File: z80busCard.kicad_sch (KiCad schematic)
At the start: 14 parts, among them J1 Conn_02x20_Odd_Even, J2 Conn_02x20_Odd_Even, J3 Conn_02x20_Odd_Even, J4 Conn_02x20_Odd_Even, J5 USB_C_Receptacle_PowerOnly_6P, SW1 SW_Push

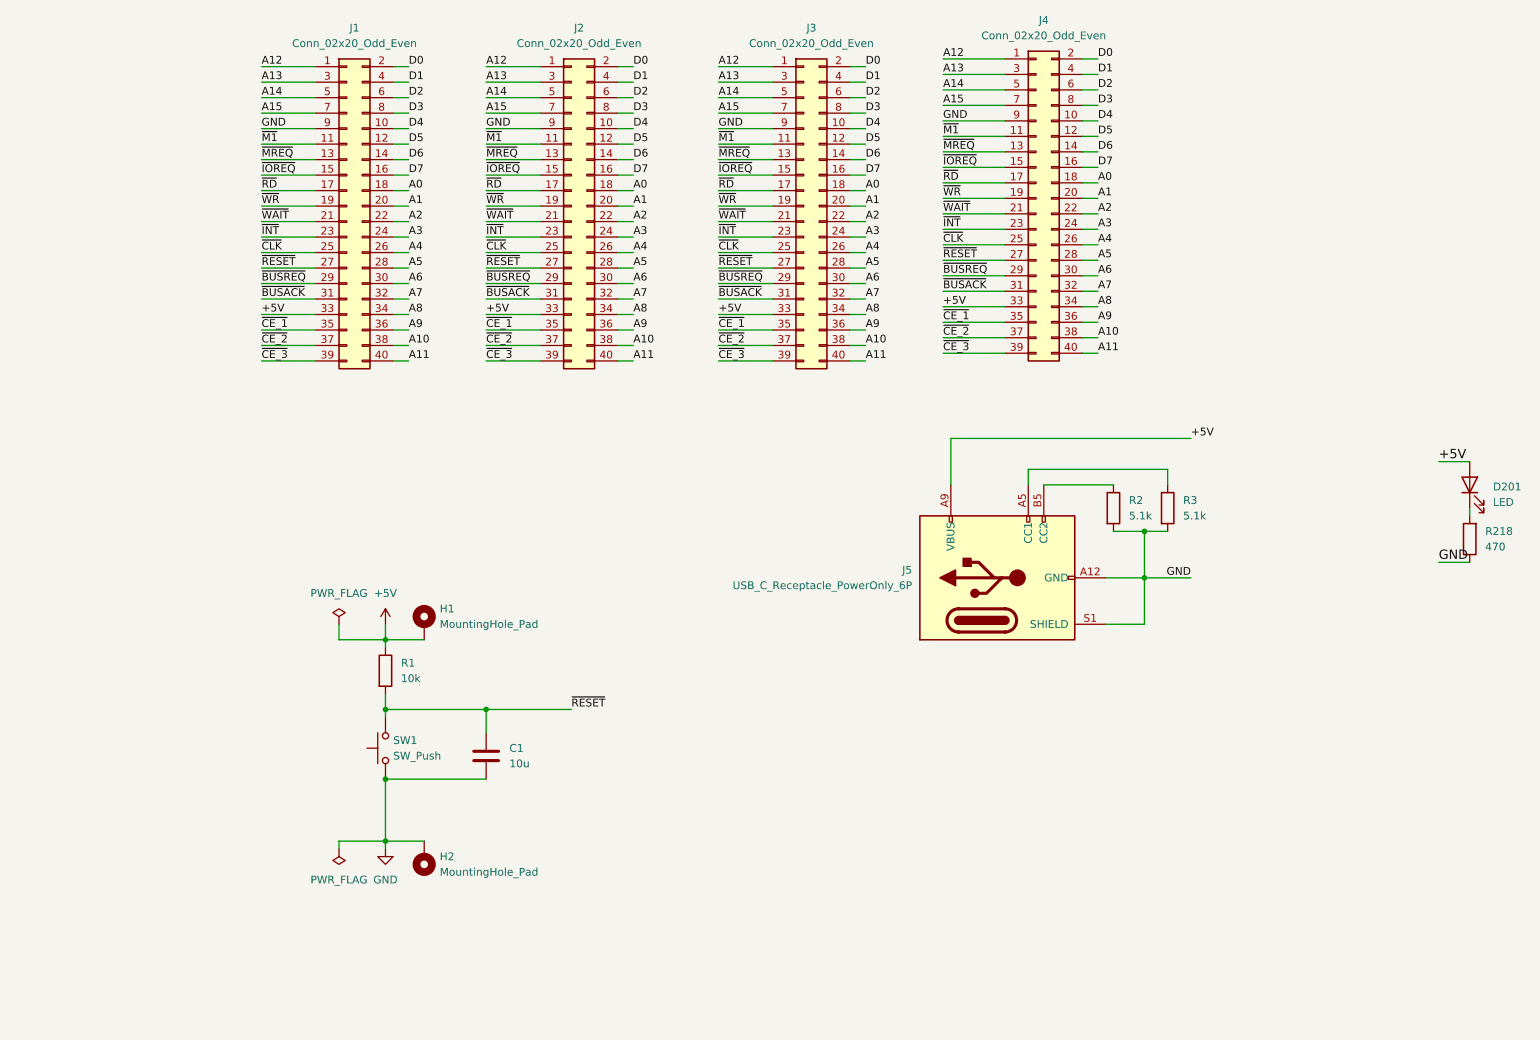
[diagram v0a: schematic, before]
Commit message: Add RESET inputs and signal conditioning
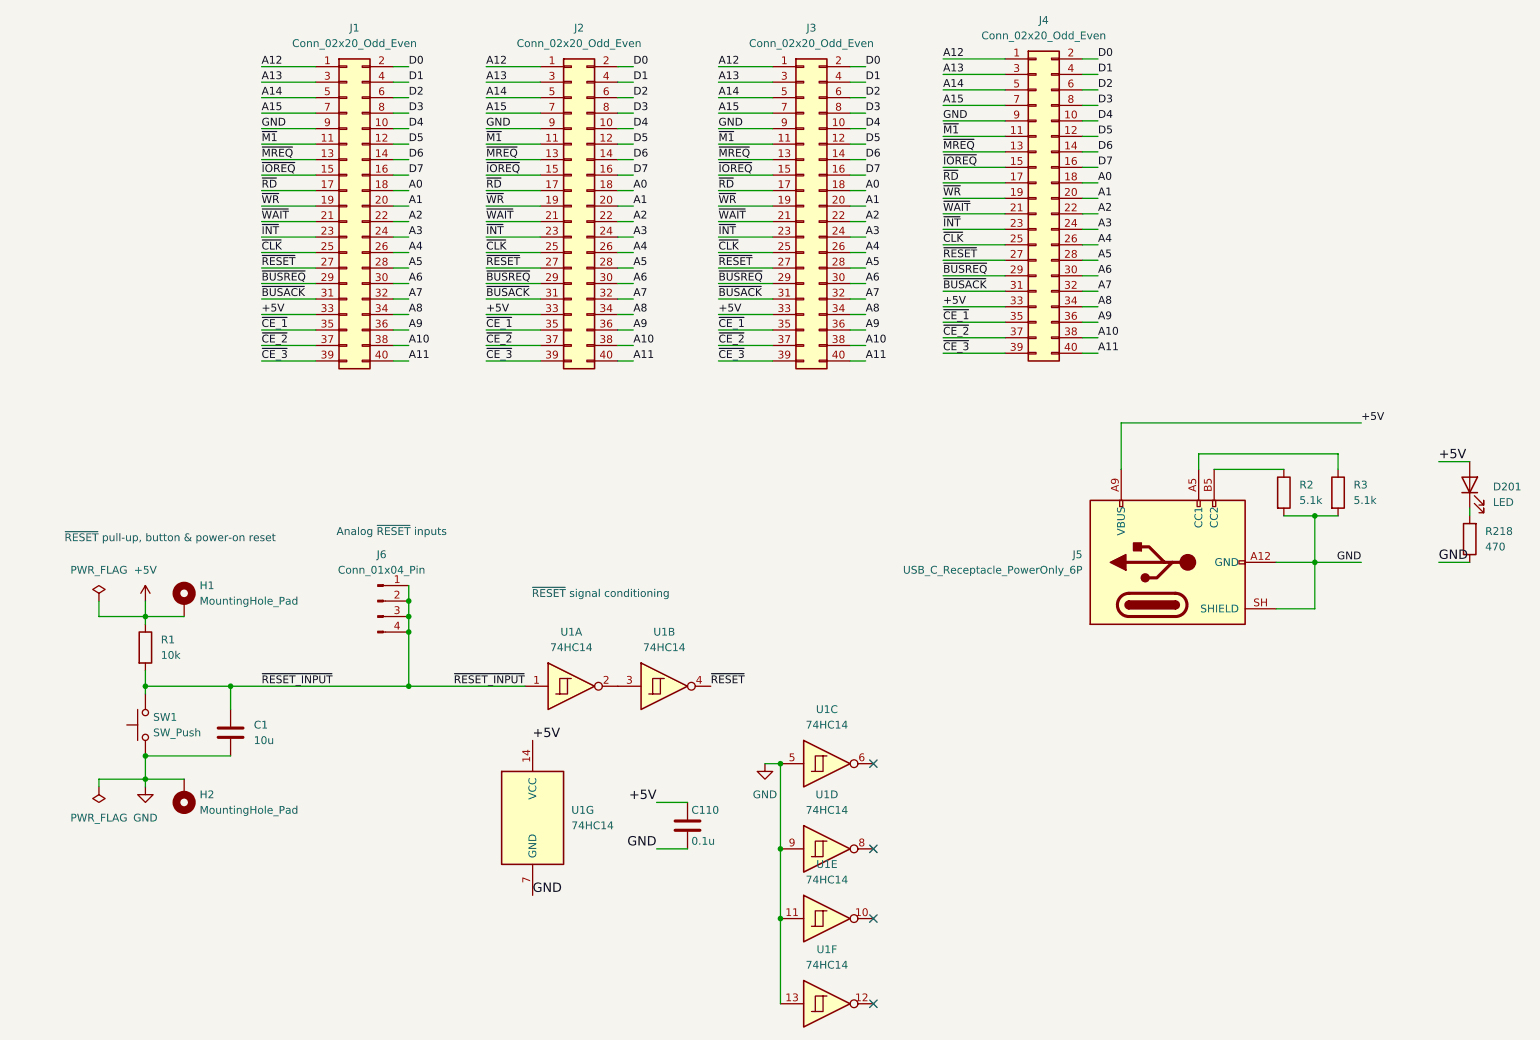
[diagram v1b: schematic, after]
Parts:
- added C110: 0.1u, Capacitor_SMD:C_0805_2012Metric_Pad1.18x1.45mm_HandSolder, symbol Device:C
- added J6: Conn_01x04_Pin, Connector_PinHeader_2.54mm:PinHeader_1x04_P2.54mm_Vertical, symbol Connector:Conn_01x04_Pin
- added U1: 74HC14, Package_DIP:DIP-14_W7.62mm_Socket, symbol 74xx:74HC14
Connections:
- net +5V: now also C110.1, U1.14 (VCC)
- net GND: now also J5.SH (SHIELD), C110.2, U1.11, U1.13, U1.5, U1.7 (GND), U1.9; no longer J5.S1 (SHIELD)
- net ~{RESET}: now also U1.4; no longer C1.1, R1.2, SW1.2
- new net: U1.2, U1.3
- new net ~{RESET_INPUT}: C1.1, J6.1 (Pin_1), J6.2 (Pin_2), J6.3 (Pin_3), J6.4 (Pin_4), R1.2, SW1.2, U1.1
- no-connect marks 0 -> 4
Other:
- note added: "Analog ~{RESET} inputs"
- note added: "~{RESET} pull-up, button & power-on reset"
- note added: "~{RESET} signal conditioning"
- moved on the sheet: C1, H1, H2, J5, R1, R2, R3, SW1

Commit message: Remove power on reset capacitor
Previously had a 10uF capacitor to GND in parallel with the switch for
automatic power on reset. That effectively smoothed out an incoming low
analog ~{RESET} signal and was therefore removed.
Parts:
- removed C1: 10u, Capacitor_SMD:C_0805_2012Metric_Pad1.18x1.45mm_HandSolder, symbol Device:C
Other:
- note added: "Note: Previously had a 10uF capacitor to GND in parallel with the switch for automatic power on reset. That effectively smoothed out an incoming low analog ~{RESET} signal and was therefore removed."
- note added: "~{RESET} pull-up & button"
- note removed: "~{RESET} pull-up, button & power-on reset"
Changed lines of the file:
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@@
 	(generator_version "10.0")
 	(paper "A4")
-	(text "~{RESET} pull-up, button & power-on reset"
+	(text "Note: Previously had a 10uF capacitor to GND in parallel \nwith the switch for automatic power on reset. That \neffectively smoothed out an incoming low analog ~{RESET} \nsignal and was therefore removed."
+		(exclude_from_sim no)
+		(at 42.672 164.084 0)
+		(effects
+			(font
+				(size 0.762 0.762)
+			)
+			(justify left)
+		)
+	)
+	(text "~{RESET} pull-up & button"
 		(exclude_from_sim no)
 		(at 34.544 133.35 0)
@@
 	)
 	(junction
-		(at 30.48 168.91)
-		(diameter 0)
-		(color 0 0 0 0)
-	)
-	(junction
 		(at 73.66 157.48)
 		(diameter 0)
@@
 		(color 0 0 0 0)
 	)
-	(junction
-		(at 44.45 157.48)
-		(diameter 0)
-		(color 0 0 0 0)
-	)
 	(no_connect
 		(at 149.86 209.55)
@@
 	(wire
 		(pts
-			(xy 44.45 161.29) (xy 44.45 157.48)
-		)
-		(stroke
-			(width 0)
-			(type default)
-		)
-	)
-	(wire
-		(pts
 			(xy 30.48 146.05) (xy 30.48 147.32)
 		)
@@
 	(wire
 		(pts
-			(xy 44.45 157.48) (xy 73.66 157.48)
+			(xy 30.48 157.48) (xy 73.66 157.48)
 		)
 		(stroke
@@
 	(wire
 		(pts
-			(xy 44.45 157.48) (xy 30.48 157.48)
-		)
-		(stroke
-			(width 0)
-			(type default)
-		)
-	)
-	(wire
-		(pts
 			(xy 184.15 72.39) (xy 186.69 72.39)
 		)
@@
 	(wire
 		(pts
-			(xy 30.48 168.91) (xy 44.45 168.91)
-		)
-		(stroke
-			(width 0)
-			(type default)
-		)
-	)
-	(wire
-		(pts
 			(xy 71.12 96.52) (xy 73.66 96.52)
 		)
@@
 				)
 			)
-		)
-	)
-	(symbol
-		(lib_id "Device:C")
-		(at 44.45 165.1 0)
-		(unit 1)
-		(body_style 1)
-		(exclude_from_sim no)
-		(in_bom yes)
-		(on_board yes)
-		(in_pos_files yes)
-		(dnp no)
-		(fields_autoplaced yes)
-		(property "Reference" "C1"
-			(at 48.26 163.8299 0)
-			(show_name no)
-			(do_not_autoplace no)
-			(effects
-				(font
-					(size 1.27 1.27)
-				)
-				(justify left)
-			)
-		)
-		(property "Value" "10u"
-			(at 48.26 166.3699 0)
-			(show_name no)
-			(do_not_autoplace no)
-			(effects
-				(font
-					(size 1.27 1.27)
-				)
-				(justify left)
-			)
-		)
-		(property "Footprint" "Capacitor_SMD:C_0805_2012Metric_Pad1.18x1.45mm_HandSolder"
-			(at 45.4152 168.91 0)
-			(hide yes)
-			(show_name no)
-			(do_not_autoplace no)
-			(effects
-				(font
-					(size 1.27 1.27)
-				)
-			)
-		)
-		(property "Datasheet" ""
-			(at 44.45 165.1 0)
-			(hide yes)
-			(show_name no)
-			(do_not_autoplace no)
-			(effects
-				(font
-					(size 1.27 1.27)
-				)
-			)
-		)
-		(property "Description" "Unpolarized capacitor"
-			(at 44.45 165.1 0)
-			(hide yes)
-			(show_name no)
-			(do_not_autoplace no)
-			(effects
-				(font
-					(size 1.27 1.27)
-				)
-			)
-		)
-		(pin "2"
-		)
-		(pin "1"
-		)
-		(instances
-			(project "z80busCard"
-				(path "/38e6c7dd-e4e5-4fac-a332-e7467610bd5b"
-					(reference "C1")
-					(unit 1)
-				)
-			)
